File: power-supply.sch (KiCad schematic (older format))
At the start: 104 parts, among them IC1 TPS54561, J12 S2B-PH-K-S_LF__SN_, Q1 BSS138APW, Q2 BSS138APW, Q3 BSS138APW, Q4 BSS138APW, Q5 BSS138APW, U10 TPS62823DLCT, U11 TPS62823DLCT, U12 TPS62823DLCT, U13 TPS62823DLCT, U9 LM3881MME_NOPB

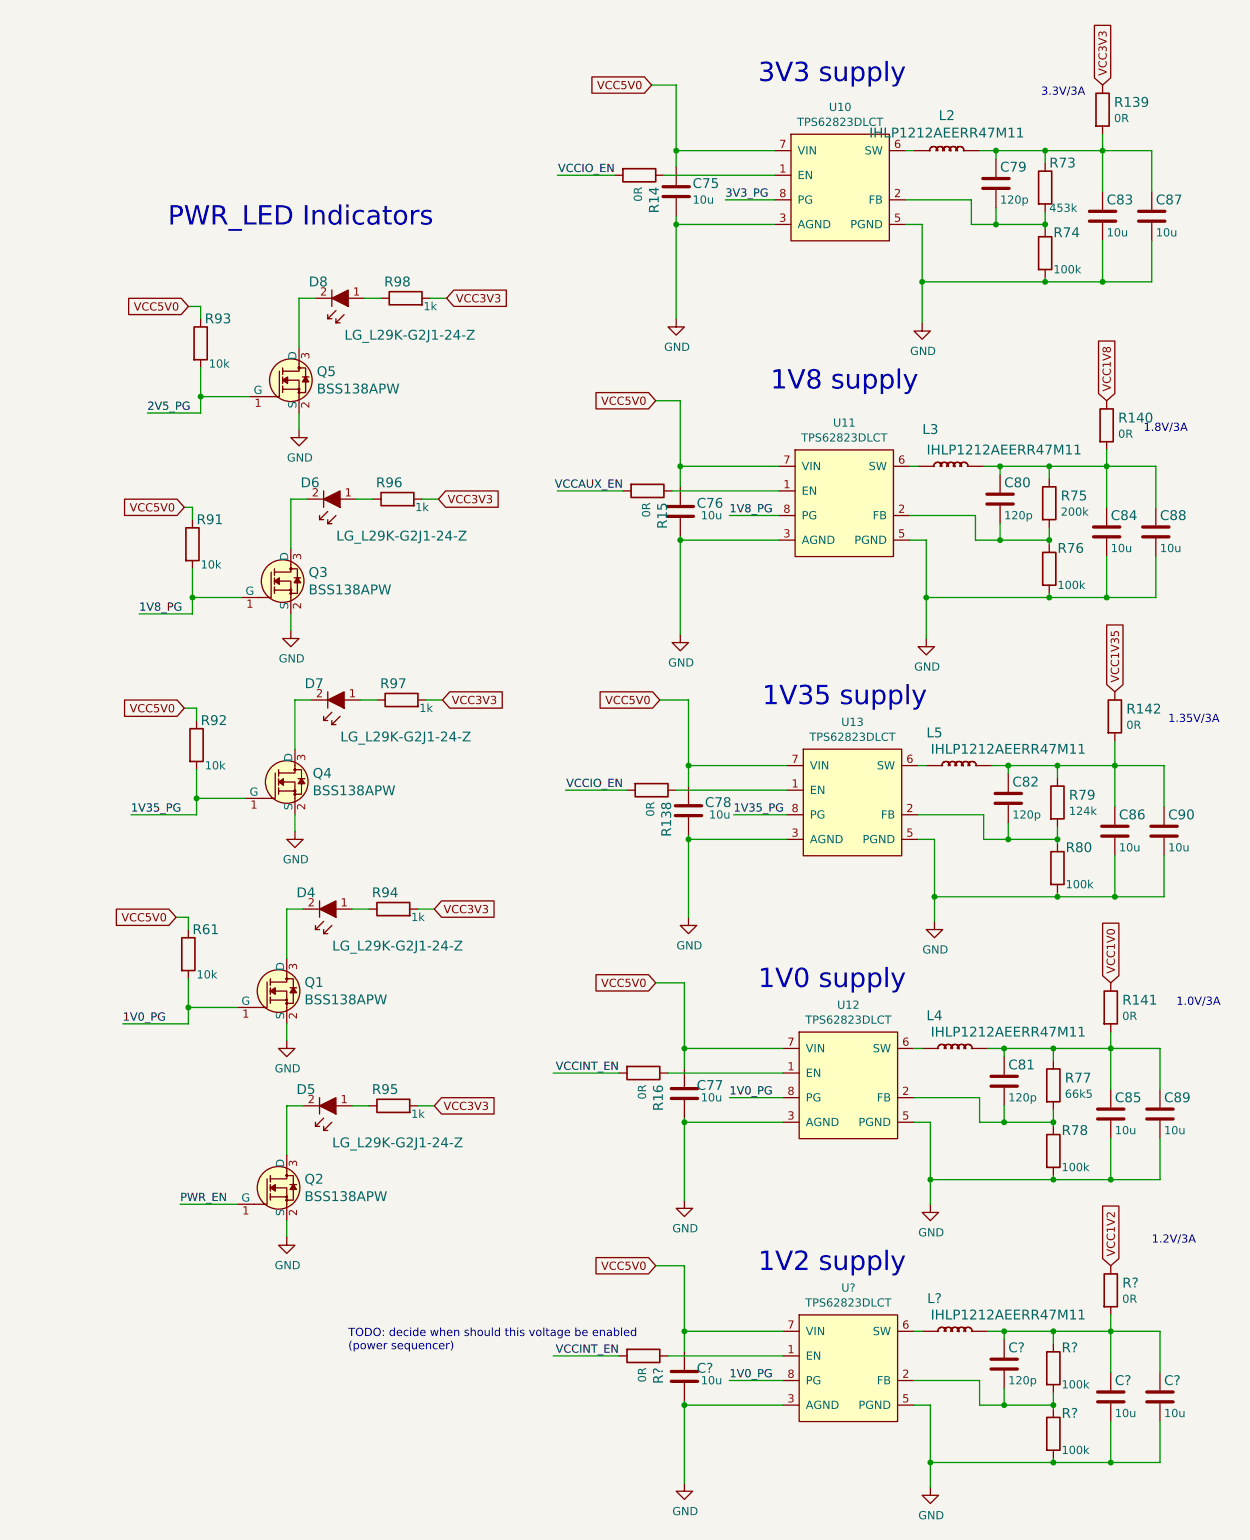
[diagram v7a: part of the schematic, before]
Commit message: Added 1V2 led indicator
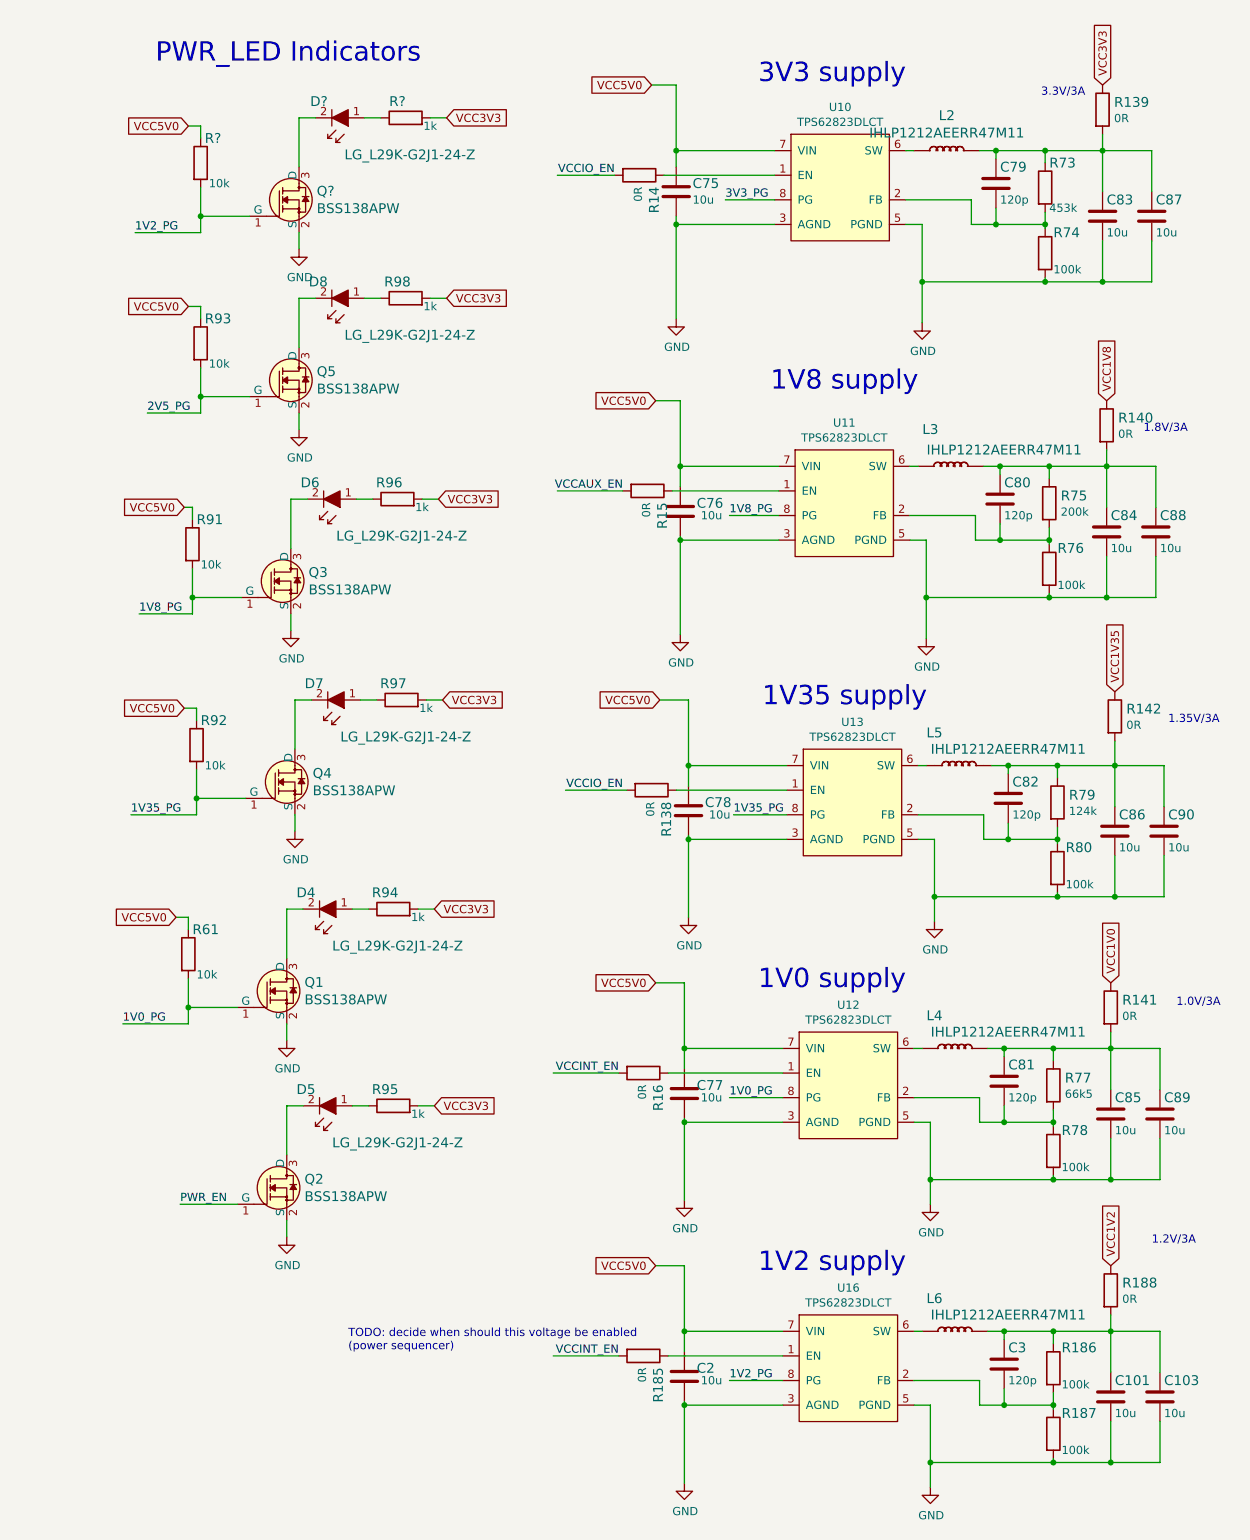
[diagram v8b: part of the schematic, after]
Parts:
- added D?: LG_L29K-G2J1-24-Z, artix-dc-scm-footprints:LED_0603, symbol artix-dc-scm:LG_L29K-G2J1-24-Z
- added Q?: BSS138APW, antmicro-footprints:SC70-3, symbol antmicroTransistorsFETsMOSFETsSingle:BSS138APW
- added R?: R_10k_0402, artix-dc-scm-footprints:0402-res, symbol artix-dc-scm:R_10k_0402
- added R?: R_1k_0402, artix-dc-scm-footprints:0402-res, symbol artix-dc-scm:R_1k_0402
- gave numbers to parts that had none: 10
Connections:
- net 1V0_PG: no longer U16.8 (PG)
- net GND: now also Q?.2 (S)
- net VCC3V3: now also R?.2
- net VCC5V0: now also R?.1
- new net: D?.1, R?.1
- new net: D?.2, Q?.3 (D)
- new net 1V2_PG: Q?.1 (G), R?.2, U16.8 (PG)
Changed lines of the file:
@@
 	1    0    0    -1
 $EndComp
-Text Notes 9525 1825 0    118  ~ 0
+Text Notes 9450 825  0    118  ~ 0
 PWR_LED Indicators
 Wire Notes Line
@@
 Connection ~ 12675 8550
 $Comp
-L artix-dc-scm:GND-artix-dc-scm #PWR?
+L artix-dc-scm:GND-artix-dc-scm #PWR04
 U 1 1 601362A3
 P 12675 9475
-F 0 "#PWR?" H 12675 9225 50  0001 C CNN
+F 0 "#PWR04" H 12675 9225 50  0001 C CNN
 F 1 "GND" H 12680 9302 50  0000 C CNN
 F 2 "" H 12675 9475 50  0001 C CNN
@@
 	14175 9000 14075 9000
 Text Label 12950 8850 0    50   ~ 0
-1V0_PG
+1V2_PG
 Wire Wire Line
 	14175 9350 14925 9350
@@
 	14625 8550 14925 8550
 $Comp
-L artix-dc-scm:C_10u_0402 C?
+L artix-dc-scm:C_10u_0402 C2
 U 1 1 601362C1
 P 12675 8825
-F 0 "C?" H 12750 8875 60  0000 L CNN
+F 0 "C2" H 12750 8875 60  0000 L CNN
 F 1 "C_10u_0402" H 12675 8675 60  0001 C CNN
 F 2 "artix-dc-scm-footprints:0402-cap" H 12875 9025 60  0001 L CNN
@@
 	12675 8150 12675 8550
 $Comp
-L artix-dc-scm:TPS62823DLCT U?
+L artix-dc-scm:TPS62823DLCT U16
 U 1 1 601362CD
 P 13625 9050
-F 0 "U?" H 13675 9815 50  0000 C CNN
+F 0 "U16" H 13675 9815 50  0000 C CNN
 F 1 "TPS62823DLCT" H 13675 9724 50  0000 C CNN
 F 2 "artix-dc-scm-footprints:QFN-8_2x1mm" H 13525 8850 50  0001 C CNN
@@
 	12675 9000 12675 9475
 $Comp
-L artix-dc-scm:C_120p_0402 C?
+L artix-dc-scm:C_120p_0402 C3
 U 1 1 601362DA
 P 14625 8750
-F 0 "C?" H 14650 8850 60  0000 L CNN
+F 0 "C3" H 14650 8850 60  0000 L CNN
 F 1 "C_120p_0402" H 14625 8600 60  0001 C CNN
 F 2 "artix-dc-scm-footprints:0402-res" H 14825 8950 60  0001 L CNN
@@
 	14925 8925 14925 9000
 $Comp
-L artix-dc-scm:R_100k_0402 R?
+L artix-dc-scm:R_100k_0402 R187
 U 1 1 601362E7
 P 14925 9175
-F 0 "R?" V 14800 9225 60  0000 L CNN
+F 0 "R187" V 14800 9225 60  0000 L CNN
 F 1 "R_100k_0402" H 14925 9025 60  0001 C CNN
 F 2 "artix-dc-scm-footprints:0402-res" H 15125 9375 60  0001 L CNN
@@
 	14925 9325 14925 9350
 $Comp
-L artix-dc-scm:C_10u_0402 C?
+L artix-dc-scm:C_10u_0402 C101
 U 1 1 601362F2
 P 15275 8950
-F 0 "C?" H 15300 9050 60  0000 L CNN
+F 0 "C101" H 15300 9050 60  0000 L CNN
 F 1 "C_10u_0402" H 15275 8800 60  0001 C CNN
 F 2 "artix-dc-scm-footprints:0402-cap" H 15475 9150 60  0001 L CNN
@@
 	15275 9100 15275 9350
 $Comp
-L artix-dc-scm:C_10u_0402 C?
+L artix-dc-scm:C_10u_0402 C103
 U 1 1 601362FE
 P 15575 8950
-F 0 "C?" H 15600 9050 60  0000 L CNN
+F 0 "C103" H 15600 9050 60  0000 L CNN
 F 1 "C_10u_0402" H 15575 8800 60  0001 C CNN
 F 2 "artix-dc-scm-footprints:0402-cap" H 15775 9150 60  0001 L CNN
@@
 	14175 9500 14175 9350
 $Comp
-L artix-dc-scm:GND-artix-dc-scm #PWR?
+L artix-dc-scm:GND-artix-dc-scm #PWR05
 U 1 1 6013630B
 P 14175 9500
-F 0 "#PWR?" H 14175 9250 50  0001 C CNN
+F 0 "#PWR05" H 14175 9250 50  0001 C CNN
 F 1 "GND" H 14180 9327 50  0000 C CNN
 F 2 "" H 14175 9500 50  0001 C CNN
@@
 	12675 8550 13275 8550
 $Comp
-L artix-dc-scm:R_0R_0402 R?
+L artix-dc-scm:R_0R_0402 R185
 U 1 1 60136320
 P 12425 8700
-F 0 "R?" V 12334 8770 60  0000 L CNN
+F 0 "R185" V 12334 8770 60  0000 L CNN
 F 1 "R_0R_0402" H 12425 8550 60  0001 C CNN
 F 2 "artix-dc-scm-footprints:0402-res" H 12625 8900 60  0001 L CNN
@@
 	12275 8700 11875 8700
 $Comp
-L antmicroFixedInductors:IHLP1212AEERR47M11 L?
+L antmicroFixedInductors:IHLP1212AEERR47M11 L6
 U 1 1 6013632B
 P 14325 8550
-F 0 "L?" H 14200 8750 60  0000 C CNN
+F 0 "L6" H 14200 8750 60  0000 C CNN
 F 1 "IHLP1212AEERR47M11" H 14650 8650 60  0000 C CNN
 F 2 "antmicro-footprints:IHLP-1212AE" H 14325 8550 60  0001 C CNN
@@
 $EndComp
 $Comp
-L antmicroResistors0603:R_0R_0603 R?
+L antmicroResistors0603:R_0R_0603 R188
 U 1 1 60136334
 P 15275 8300
-F 0 "R?" V 15230 8370 60  0000 L CNN
+F 0 "R188" V 15230 8370 60  0000 L CNN
 F 1 "R_0R_0603" H 15275 8150 60  0001 C CNN
 F 2 "antmicro-footprints:0603-res" H 15475 8500 60  0001 L CNN
@@
 TODO: decide when should this voltage be enabled\n(power sequencer)
 $Comp
-L artix-dc-scm:R_100k_0402 R?
+L artix-dc-scm:R_100k_0402 R186
 U 1 1 6021195E
 P 14925 8775
-F 0 "R?" V 14800 8825 60  0000 L CNN
+F 0 "R186" V 14800 8825 60  0000 L CNN
 F 1 "R_100k_0402" H 14925 8625 60  0001 C CNN
 F 2 "artix-dc-scm-footprints:0402-res" H 15125 8975 60  0001 L CNN
@@
 	0    1    1    0
 $EndComp
+Wire Wire Line
+	9725 1200 9650 1200
+Wire Wire Line
+	9725 1750 10025 1750
+Wire Wire Line
+	10325 1150 10325 1450
+$Comp
+L artix-dc-scm:R_10k_0402 R?
+U 1 1 60252526
+P 9725 1425
+F 0 "R?" V 9575 1450 60  0000 L CNN
+F 1 "R_10k_0402" H 9725 1275 60  0001 C CNN
+F 2 "artix-dc-scm-footprints:0402-res" H 9925 1625 60  0001 L CNN
+F 3 "" H 9725 1425 50  0001 C CNN
+F 4 "VISHAY" H 9925 1825 60  0001 L CNN "Manufacturer"
+F 5 "CRCW040210K0FKEDHP" H 9925 1725 60  0001 L CNN "MPN"
+F 6 "10k" V 9850 1475 50  0000 L CNN "Val"
+	1    9725 1425
+	0    1    1    0
+$EndComp
+Wire Wire Line
+	9725 1200 9725 1275
+Wire Wire Line
+	9725 1575 9725 1750
+$Comp
+L artix-dc-scm:LG_L29K-G2J1-24-Z D?
+U 1 1 60252530
+P 10525 1150
+F 0 "D?" H 10550 1050 60  0000 L CNN
+F 1 "LG_L29K-G2J1-24-Z" H 9650 1375 60  0000 L CNN
+F 2 "artix-dc-scm-footprints:LED_0603" H 10725 1350 60  0001 L CNN
+F 3 "https://dammedia.osram.info/media/resource/hires/osram-dam-2493945/LG%20L29K.pdf" H 10725 1450 60  0001 L CNN
+F 4 "LG L29K-G2J1-24-Z" H 10725 1650 60  0001 L CNN "MPN"
+F 5 "OSRAM Opto Semiconductors Inc." H 10725 2250 60  0001 L CNN "Manufacturer"
+	1    10525 1150
+	-1   0    0    1
+$EndComp
+Wire Wire Line
+	10325 1150 10425 1150
+Wire Wire Line
+	10725 1150 10825 1150
+$Comp
+L artix-dc-scm:R_1k_0402 R?
+U 1 1 6025253B
+P 10975 1150
+F 0 "R?" H 10925 1250 60  0000 C CNN
+F 1 "R_1k_0402" H 10975 1000 60  0001 C CNN
+F 2 "artix-dc-scm-footprints:0402-res" H 11175 1350 60  0001 L CNN
+F 3 "" H 10975 1150 50  0001 C CNN
+F 4 "BOURNS" H 11175 1550 60  0001 L CNN "Manufacturer"
+F 5 "CR0402-FX-1001GLF" H 11175 1450 60  0001 L CNN "MPN"
+F 6 "1k" H 11125 1100 50  0000 C CNN "Val"
+	1    10975 1150
+	1    0    0    -1
+$EndComp
+Text GLabel 11225 1150 2    50   Input ~ 0
+VCC3V3
+Wire Wire Line
+	11125 1150 11225 1150
+$Comp
+L artix-dc-scm:GND-artix-dc-scm #PWR?
+U 1 1 60252543
+P 10325 1950
+F 0 "#PWR?" H 10325 1700 50  0001 C CNN
+F 1 "GND" H 10330 1777 50  0000 C CNN
+F 2 "" H 10325 1950 50  0001 C CNN
+F 3 "" H 10325 1950 50  0001 C CNN
+	1    10325 1950
+	1    0    0    -1
+$EndComp
+Wire Wire Line
+	10325 1950 10325 1850
+Wire Wire Line
+	9725 1750 9725 1850
+Wire Wire Line
+	9725 1850 9325 1850
+Connection ~ 9725 1750
+Text Label 9325 1850 0    50   ~ 0
+1V2_PG
+Text GLabel 9650 1200 0    50   Input ~ 0
+VCC5V0
+$Comp
+L antmicroTransistorsFETsMOSFETsSingle:BSS138APW Q?
+U 1 1 60252551
+P 10325 1650
+F 0 "Q?" H 10433 1703 60  0000 L CNN
+F 1 "BSS138APW" H 10433 1597 60  0000 L CNN
+F 2 "antmicro-footprints:SC70-3" H 10525 1850 60  0001 L CNN
+F 3 "" H 10525 1950 60  0001 L CNN
+F 4 "BSS138PW" H 10525 2150 60  0001 L CNN "MPN"
+F 5 "ON Semiconductor" H 10525 2750 60  0001 L CNN "Manufacturer"
+	1    10325 1650
+	1    0    0    -1
+$EndComp
 $EndSCHEMATC
